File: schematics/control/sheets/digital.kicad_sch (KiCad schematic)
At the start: 10 parts, among them U17 Pico, U4 6N138, U4 MCP4822

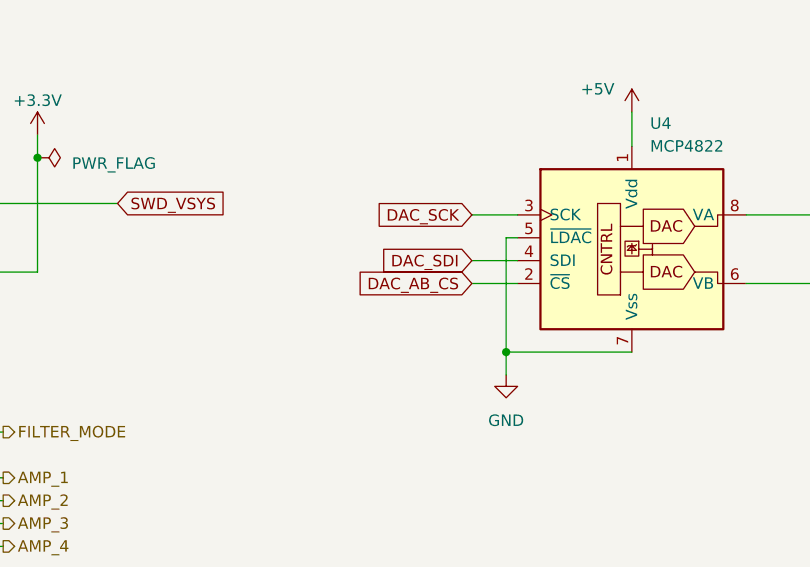
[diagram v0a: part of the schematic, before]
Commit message: Updated DCO pins
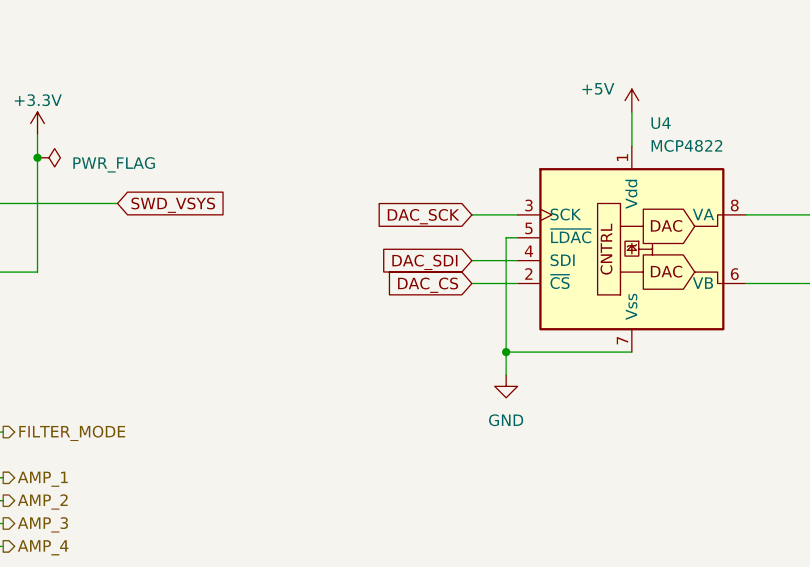
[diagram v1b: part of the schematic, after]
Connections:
- net DAC_AB_CS is gone; now on net DAC_CS: U4.2 (~{CS})
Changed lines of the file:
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@@
     )
   )
-  (global_label "DAC_AB_CS" (shape input) (at 147.32 67.31 180) (fields_autoplaced)
-    (effects (font (size 1.27 1.27)) (justify right))
-    (property "Intersheetrefs" "${INTERSHEET_REFS}" (at 134.505 67.2306 0)
+  (global_label "DAC_CS" (shape input) (at 147.32 67.31 180) (fields_autoplaced)
+    (effects (font (size 1.27 1.27)) (justify right))
+    (property "Intersheetrefs" "${INTERSHEET_REFS}" (at 137.3385 67.31 0)
       (effects (font (size 1.27 1.27)) (justify right) hide)
     )
@@
     (pin "8")
     (instances
-      (project "shmoergh-funk-livecontrol"
+      (project "shmoergh-funk-live-control"
         (path "/6d7b782d-8b2e-4b40-a99f-4bf41187d978/88d90181-522e-4756-bb1e-20cf1e1feb05"
           (reference "U4") (unit 1)
@@
         )
       )
-      (project "shmoergh-funk-livecontrol"
+      (project "shmoergh-funk-live-control"
         (path "/6d7b782d-8b2e-4b40-a99f-4bf41187d978/88d90181-522e-4756-bb1e-20cf1e1feb05"
           (reference "#J_MIDI_IN1") (unit 1)
@@
         )
       )
-      (project "shmoergh-funk-livecontrol"
+      (project "shmoergh-funk-live-control"
         (path "/6d7b782d-8b2e-4b40-a99f-4bf41187d978/88d90181-522e-4756-bb1e-20cf1e1feb05"
           (reference "#PWR0115") (unit 1)
@@
     (pin "2")
     (instances
-      (project "shmoergh-funk-livecontrol"
+      (project "shmoergh-funk-live-control"
         (path "/6d7b782d-8b2e-4b40-a99f-4bf41187d978/88d90181-522e-4756-bb1e-20cf1e1feb05"
           (reference "D3") (unit 1)
@@
     (pin "9")
     (instances
-      (project "shmoergh-funk-livecontrol"
+      (project "shmoergh-funk-live-control"
         (path "/6d7b782d-8b2e-4b40-a99f-4bf41187d978/88d90181-522e-4756-bb1e-20cf1e1feb05"
           (reference "U17") (unit 1)
@@
         )
       )
-      (project "shmoergh-funk-livecontrol"
+      (project "shmoergh-funk-live-control"
         (path "/6d7b782d-8b2e-4b40-a99f-4bf41187d978/88d90181-522e-4756-bb1e-20cf1e1feb05"
           (reference "#PWR0114") (unit 1)
@@
         )
       )
-      (project "shmoergh-funk-livecontrol"
+      (project "shmoergh-funk-live-control"
         (path "/6d7b782d-8b2e-4b40-a99f-4bf41187d978/88d90181-522e-4756-bb1e-20cf1e1feb05"
           (reference "R57") (unit 1)
@@
         )
       )
-      (project "shmoergh-funk-livecontrol"
+      (project "shmoergh-funk-live-control"
         (path "/6d7b782d-8b2e-4b40-a99f-4bf41187d978/88d90181-522e-4756-bb1e-20cf1e1feb05"
           (reference "R56") (unit 1)
@@
         )
       )
-      (project "shmoergh-funk-livecontrol"
+      (project "shmoergh-funk-live-control"
         (path "/6d7b782d-8b2e-4b40-a99f-4bf41187d978/88d90181-522e-4756-bb1e-20cf1e1feb05"
           (reference "J_MIDI_IN1") (unit 1)
@@
     (pin "1")
     (instances
-      (project "shmoergh-funk-livecontrol"
+      (project "shmoergh-funk-live-control"
         (path "/6d7b782d-8b2e-4b40-a99f-4bf41187d978/88d90181-522e-4756-bb1e-20cf1e1feb05"
           (reference "#PWR0112") (unit 1)
@@
         )
       )
-      (project "shmoergh-funk-livecontrol"
+      (project "shmoergh-funk-live-control"
         (path "/6d7b782d-8b2e-4b40-a99f-4bf41187d978/88d90181-522e-4756-bb1e-20cf1e1feb05"
           (reference "U18") (unit 1)
@@
     (pin "1")
     (instances
-      (project "shmoergh-funk-livecontrol"
+      (project "shmoergh-funk-live-control"
         (path "/6d7b782d-8b2e-4b40-a99f-4bf41187d978/88d90181-522e-4756-bb1e-20cf1e1feb05"
           (reference "#PWR0111") (unit 1)
@@
         )
       )
-      (project "shmoergh-funk-livecontrol"
+      (project "shmoergh-funk-live-control"
         (path "/6d7b782d-8b2e-4b40-a99f-4bf41187d978/88d90181-522e-4756-bb1e-20cf1e1feb05"
           (reference "R55") (unit 1)
@@
     (pin "1")
     (instances
-      (project "shmoergh-funk-livecontrol"
+      (project "shmoergh-funk-live-control"
         (path "/6d7b782d-8b2e-4b40-a99f-4bf41187d978/88d90181-522e-4756-bb1e-20cf1e1feb05"
           (reference "#FLG04") (unit 1)
@@
     (pin "1")
     (instances
-      (project "shmoergh-funk-livecontrol"
+      (project "shmoergh-funk-live-control"
         (path "/6d7b782d-8b2e-4b40-a99f-4bf41187d978/88d90181-522e-4756-bb1e-20cf1e1feb05"
           (reference "#PWR040") (unit 1)
@@
     (pin "1")
     (instances
-      (project "shmoergh-funk-livecontrol"
+      (project "shmoergh-funk-live-control"
         (path "/6d7b782d-8b2e-4b40-a99f-4bf41187d978/88d90181-522e-4756-bb1e-20cf1e1feb05"
           (reference "#PWR0116") (unit 1)
@@
     (pin "1")
     (instances
-      (project "shmoergh-funk-livecontrol"
+      (project "shmoergh-funk-live-control"
         (path "/6d7b782d-8b2e-4b40-a99f-4bf41187d978/88d90181-522e-4756-bb1e-20cf1e1feb05"
           (reference "#PWR0113") (unit 1)
@@
     (pin "1")
     (instances
-      (project "shmoergh-funk-livecontrol"
+      (project "shmoergh-funk-live-control"
         (path "/6d7b782d-8b2e-4b40-a99f-4bf41187d978/88d90181-522e-4756-bb1e-20cf1e1feb05"
           (reference "#PWR0117") (unit 1)
@@
         )
       )
-      (project "shmoergh-funk-livecontrol"
+      (project "shmoergh-funk-live-control"
         (path "/6d7b782d-8b2e-4b40-a99f-4bf41187d978/88d90181-522e-4756-bb1e-20cf1e1feb05"
           (reference "J_SWD_IO1") (unit 1)
@@
     (pin "1")
     (instances
-      (project "shmoergh-funk-livecontrol"
+      (project "shmoergh-funk-live-control"
         (path "/6d7b782d-8b2e-4b40-a99f-4bf41187d978/88d90181-522e-4756-bb1e-20cf1e1feb05"
           (reference "#PWR041") (unit 1)

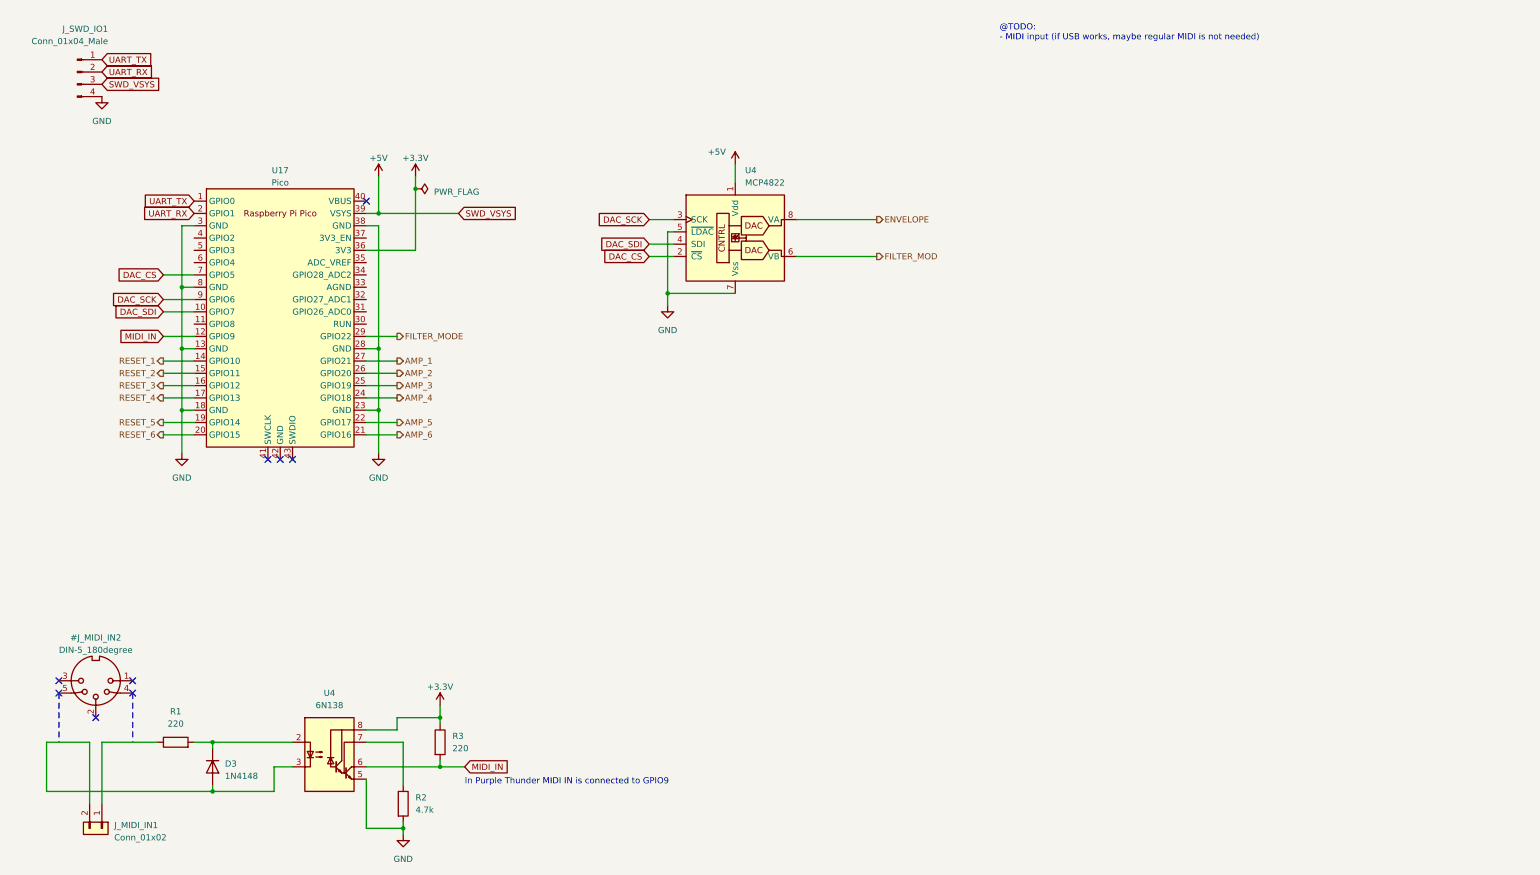
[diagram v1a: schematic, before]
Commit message: Added pulse width mod schematics
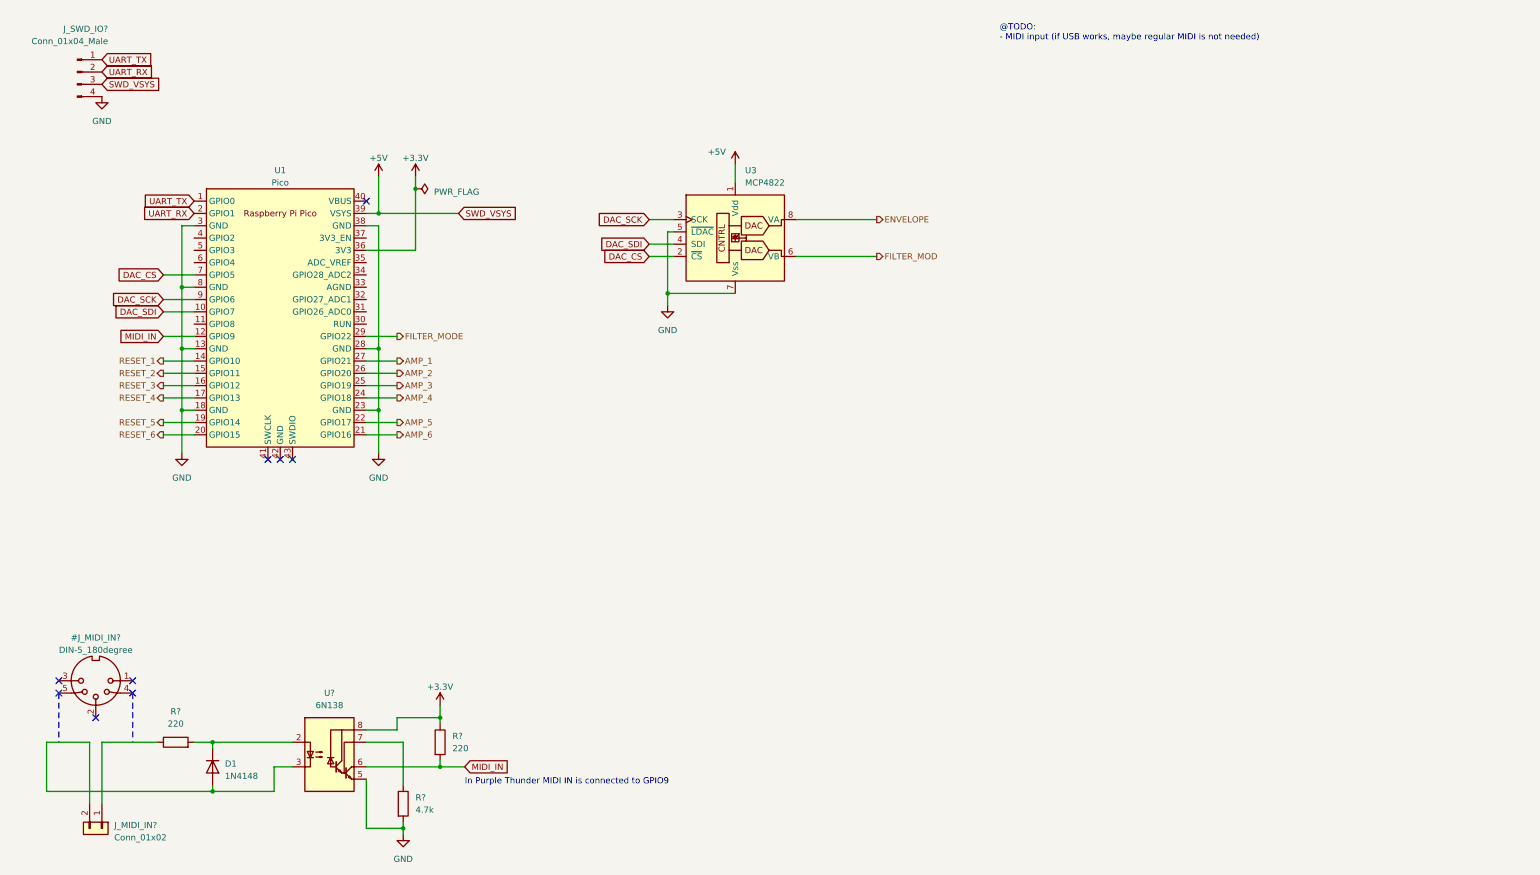
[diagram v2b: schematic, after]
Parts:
- renumbered #J_MIDI_IN2 to #J_MIDI_IN?, D3 to D1, J_MIDI_IN1 to J_MIDI_IN?, J_SWD_IO1 to J_SWD_IO?, R3 to R?, R2 to R?, R1 to R?, U17 to U1, U4 to U3, U4 to U?

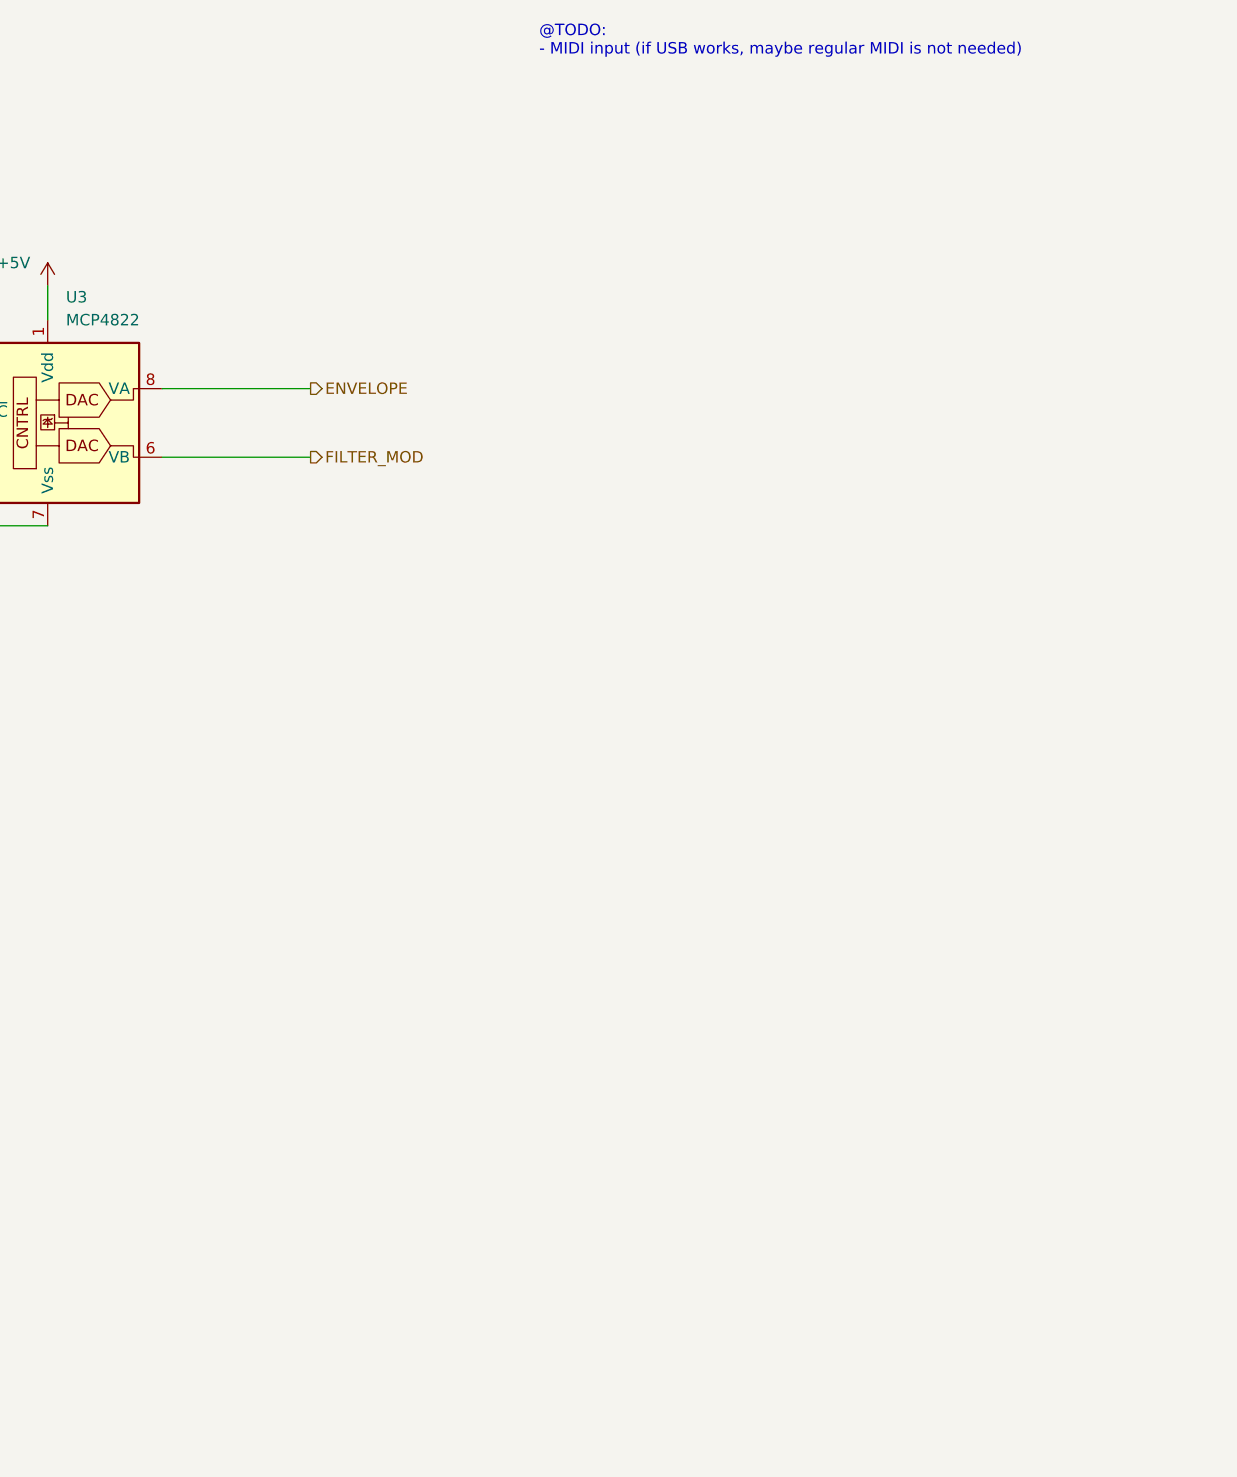
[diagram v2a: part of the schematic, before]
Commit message: Updated ADSR code and DAC schem.
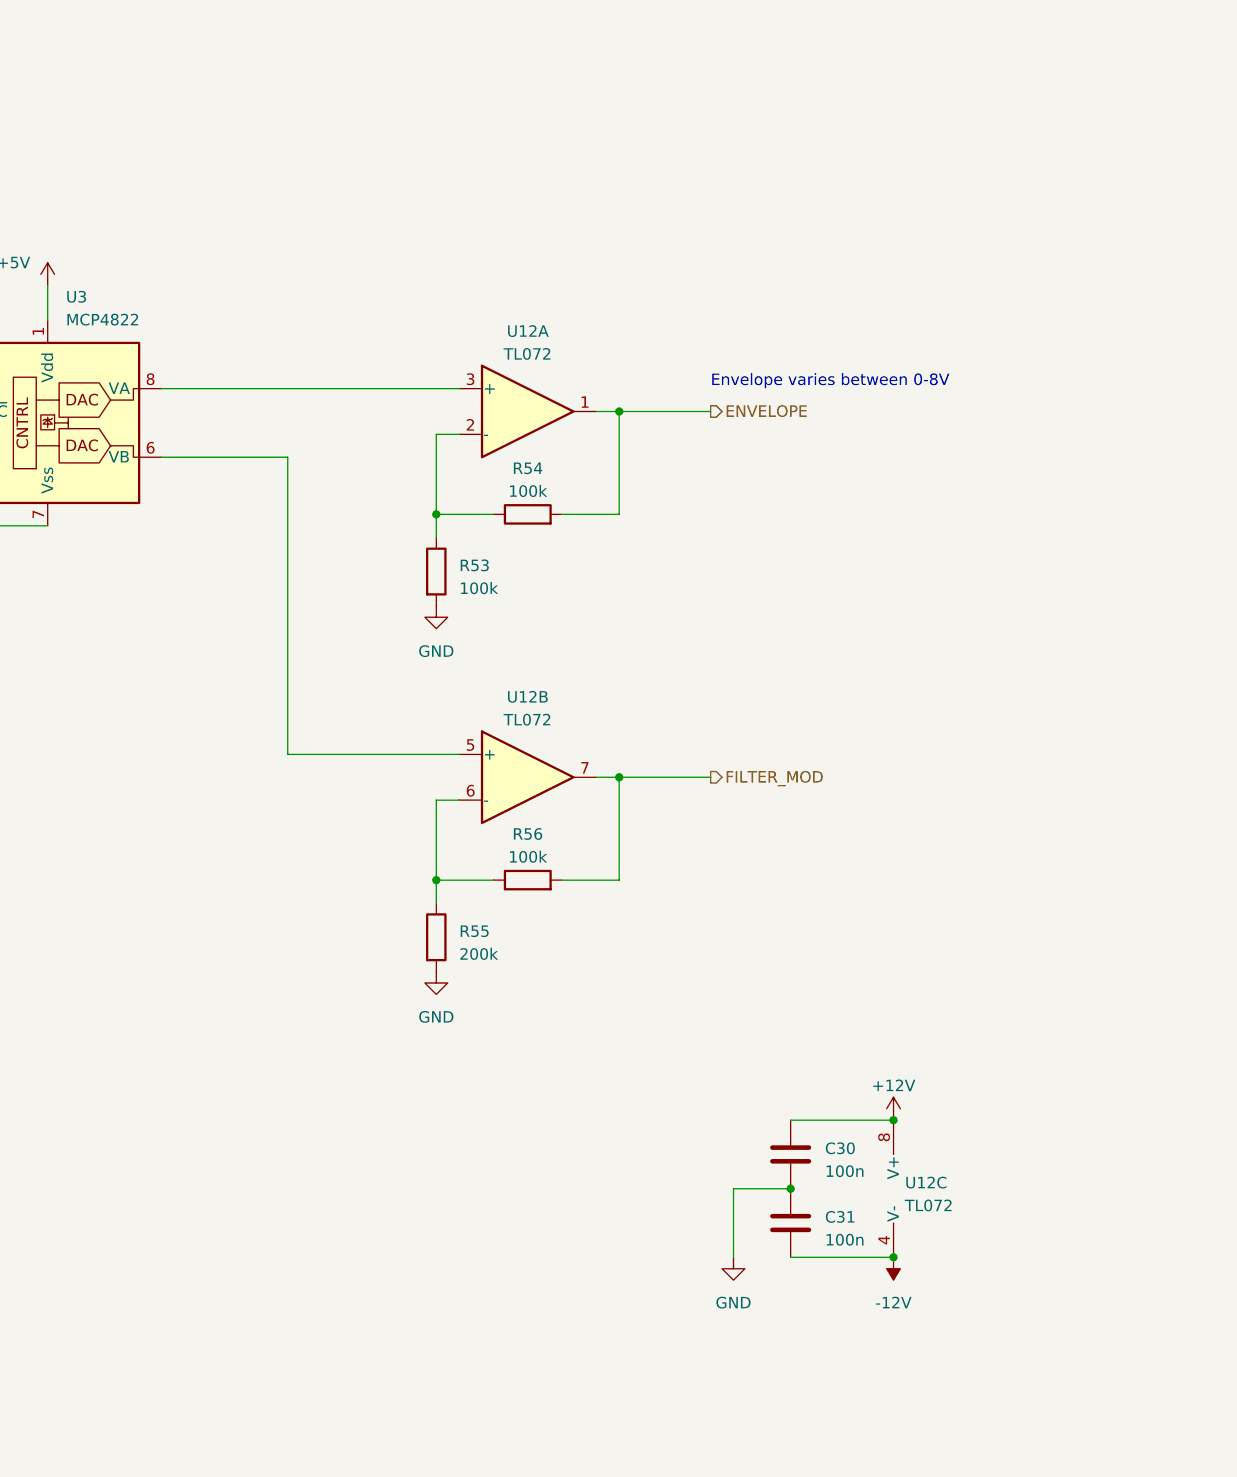
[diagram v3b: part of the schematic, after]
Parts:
- added C30, C31: 100n, symbol Device:C
- added R53, R54, R56: 100k, symbol Device:R
- added R55: 200k, symbol Device:R
- added U12: TL072, symbol Amplifier_Operational:TL072
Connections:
- net ENVELOPE: now also R54.2, U12.1; no longer U3.8 (VA)
- net FILTER_MOD: now also R56.2, U12.7; no longer U3.6 (VB)
- net GND: now also C30.2, C31.1, R53.2, R55.2
- new net: U12.5 (+), U3.6 (VB)
- new net: U12.3 (+), U3.8 (VA)
- new net: R53.1, R54.1, U12.2 (-)
- new net: R55.1, R56.1, U12.6 (-)
- new net +12V: C30.1, U12.8 (V+)
- new net -12V: C31.2, U12.4 (V-)
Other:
- note added: "Envelope varies between 0-8V"
- note removed: "@TODO: - MIDI input (if USB works, maybe regular MIDI is not needed)"
